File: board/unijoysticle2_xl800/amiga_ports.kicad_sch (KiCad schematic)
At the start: 23 parts, among them J2 DE9_Receptacle, J3 DE9_Receptacle, SW3 MODE, SW4 SWAP, U4 74HC05, U5 74HC05, U6 74HC05

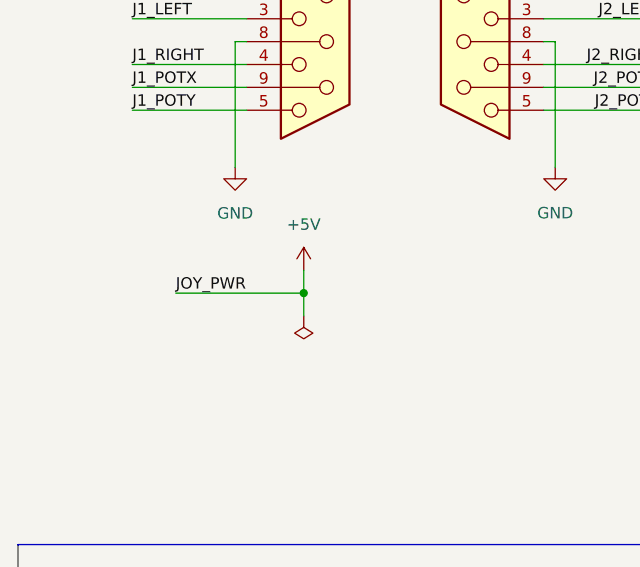
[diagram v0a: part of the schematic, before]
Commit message: 800xl: routes added
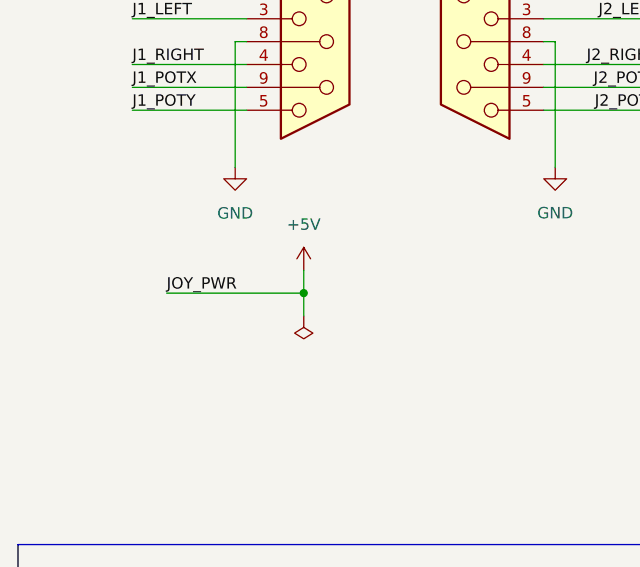
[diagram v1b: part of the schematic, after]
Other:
- title: Unijoysticle 2 A500 -> Unijoysticle 2 XL800
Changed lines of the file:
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@@
   (paper "A4")
   (title_block
-    (title "Unijoysticle 2 A500")
-    (date "2022-05-26")
-    (rev "C")
+    (title "Unijoysticle 2 XL800")
+    (date "2023-06-16")
+    (rev "A")
     (company "Ricardo Quesada")
   )
@@
     (stroke (width 0) (type default))
   )
-  (wire (pts (xy 28.956 81.28) (xy 43.18 81.28))
+  (wire (pts (xy 27.94 81.28) (xy 43.18 81.28))
     (stroke (width 0) (type default))
   )
@@
     (effects (font (size 1.27 1.27)) (justify left bottom))
   )
-  (label "JOY_PWR" (at 28.956 81.28 0) (fields_autoplaced)
-    (effects (font (size 1.27 1.27)) (justify left bottom))
-  )
+  (label "JOY_PWR" (at 27.94 81.28 0) (fields_autoplaced)
+    (effects (font (size 1.27 1.27)) (justify left bottom))
+  )

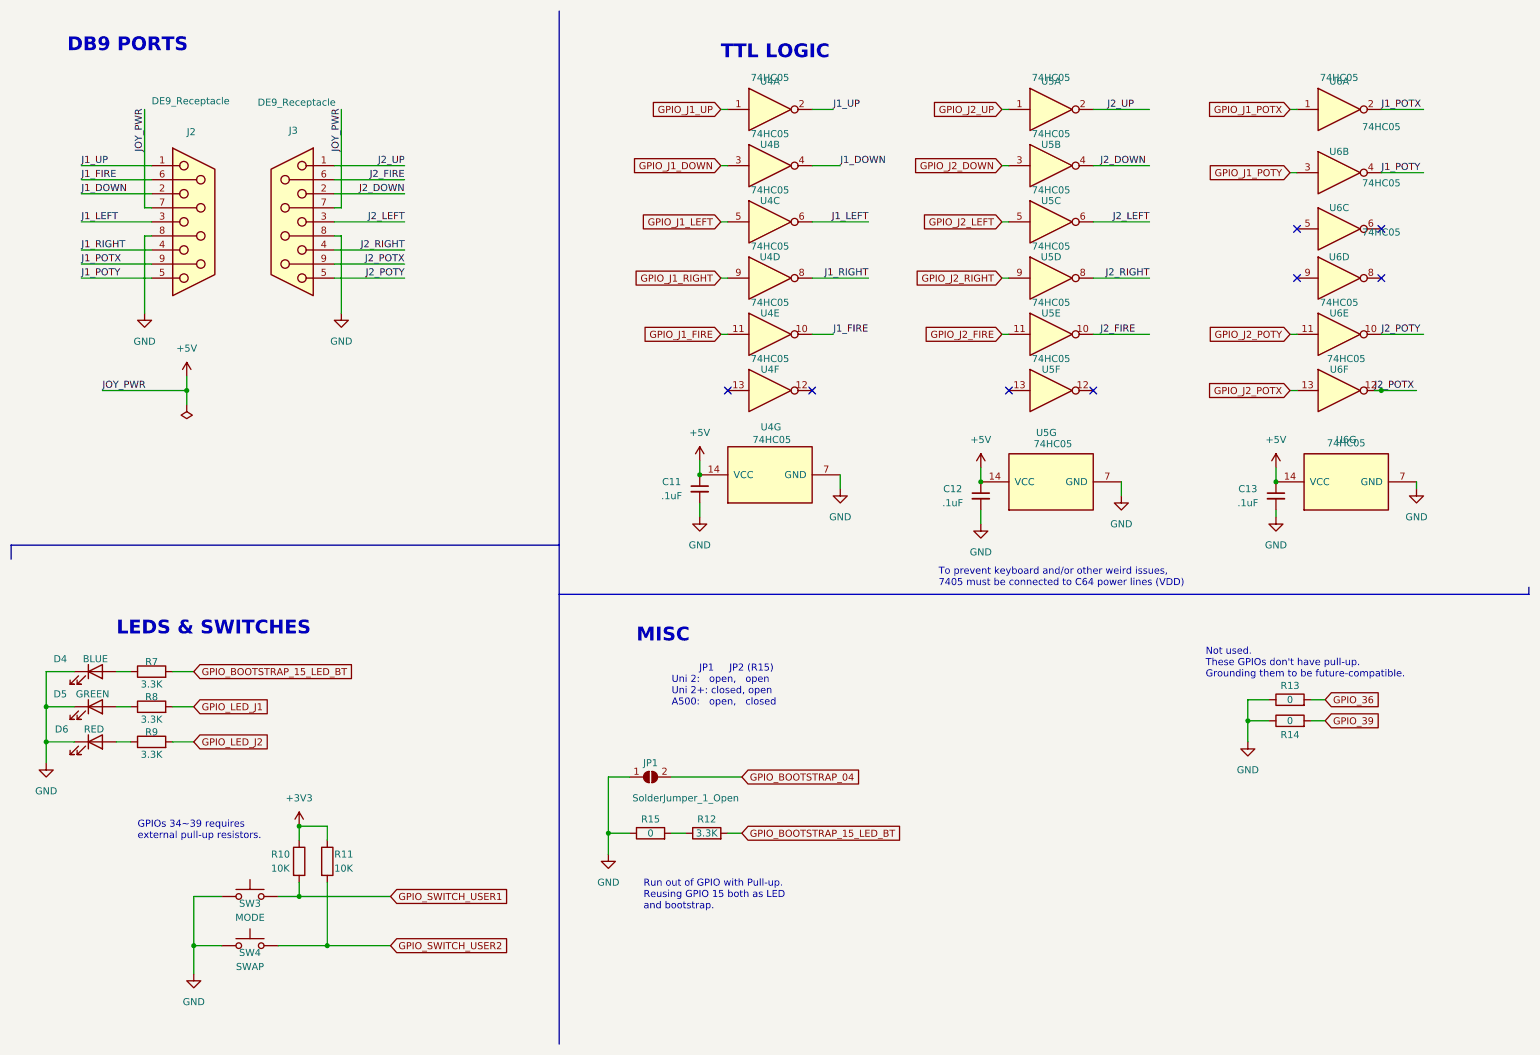
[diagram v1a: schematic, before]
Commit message: 800XL Rev B.
Support Joy2Bplus buttons: similar to C64 Pot buttons.
GPIO36 Pull-up (instead of Pull-down) so that A500 can be differenciated
from 800XL.
Rounded corners at the top: might be needed if the DE9 connectors is
cut.
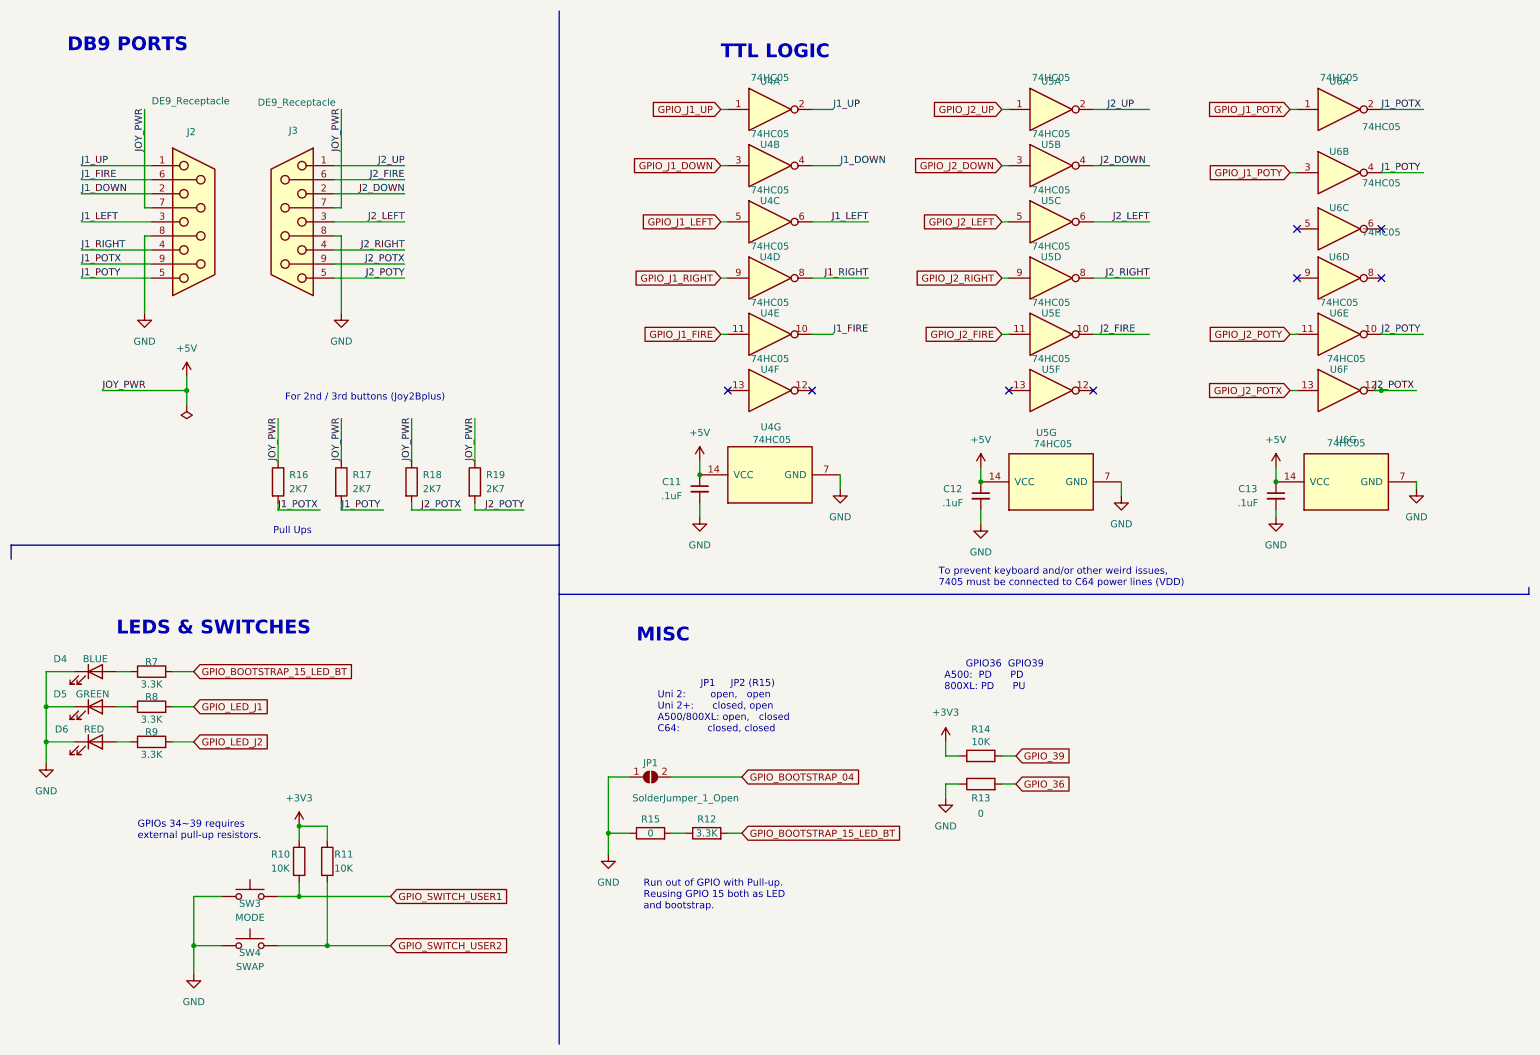
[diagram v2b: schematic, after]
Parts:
- added R16, R17, R18, R19: 2K7, Resistor_SMD:R_0805_2012Metric_Pad1.20x1.40mm_HandSolder, symbol Device:R
- R14: value 0 -> 10K
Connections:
- net +3V3: now also R14.2
- net +5V: now also R16.1, R17.1, R18.1, R19.1
- net GND: no longer R14.1
- net GPIO_39: now also R14.1; no longer R14.2
- net J1_POTX: now also R16.2
- net J1_POTY: now also R17.2
- net J2_POTX: now also R18.2
- net J2_POTY: now also R19.2
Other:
- note added: "For 2nd / 3rd buttons (Joy2Bplus)"
- note added: "GPIO36 GPIO39 A500: PD PD 800XL: PD PU"
- note added: "JP1 JP2 (R15) Uni 2: open, open Uni 2+: closed, open A500/800XL: open, closed C64: closed, closed"
- note added: "Pull Ups"
- note removed: "JP1 JP2 (R15) Uni 2: open, open Uni 2+: closed, open A500: open, closed"
- note removed: "Not used. These GPIOs don't have pull-up. Grounding them to be future-compatible."
- title: Unijoysticle 2 XL800 -> Unijoysticle 2 800XL
- moved on the sheet: R13, R14
